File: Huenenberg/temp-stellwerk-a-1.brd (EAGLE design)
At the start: 99.1 x 61 mm, 117 parts, among them Q1 BSS123, Q10 BSS84, Q11 BSS123, Q12 BSS84, Q13 BSS123, Q14 BSS84, Q15 BSS123, Q16 BSS84, Q17 BSS123, Q18 BSS84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

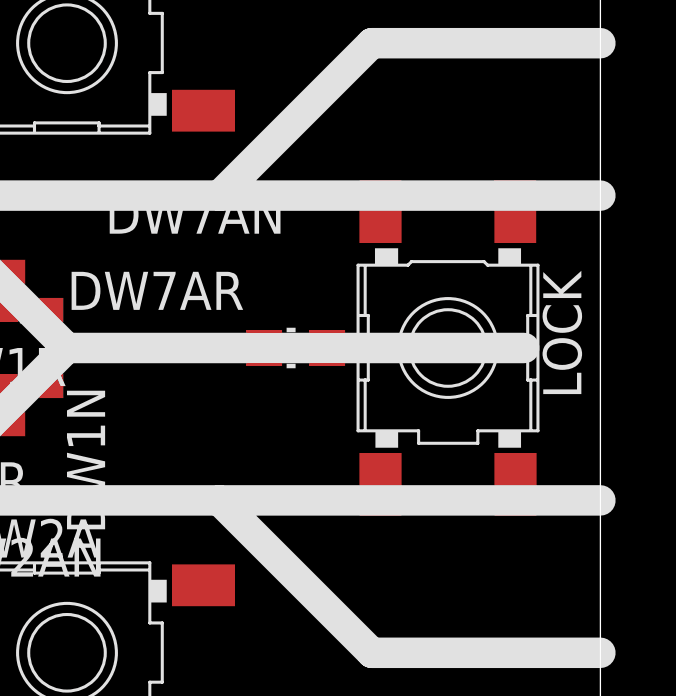
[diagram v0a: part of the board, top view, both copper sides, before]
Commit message: Updates names of all buttons.
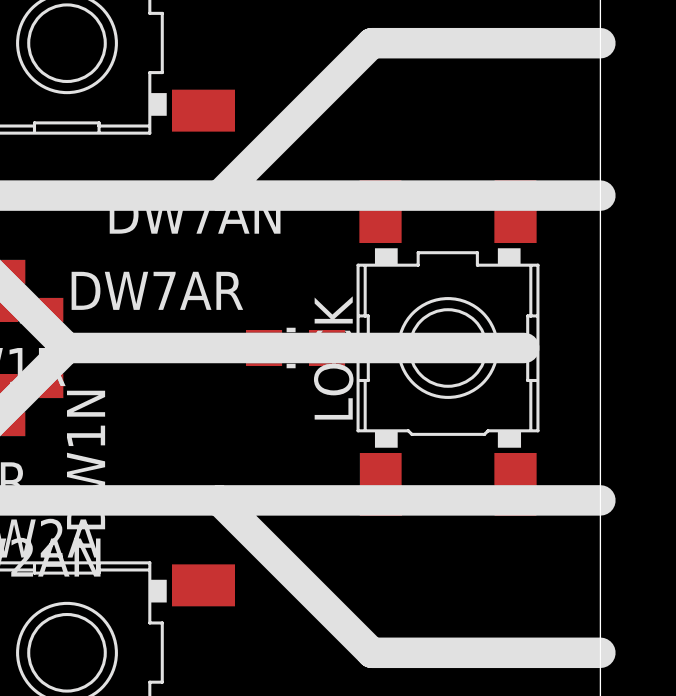
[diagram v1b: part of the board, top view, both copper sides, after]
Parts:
- LOCK: value W2 -> LOCK
- TRK1, TRK2, TRK3, TRK4, TRK5, TRK6, W2A, W7A: value W2 -> (none)
- W2B, W7B: value W1 -> (none)
- turned LOCK to 90 degrees
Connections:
- net CH10: now also Q11.1, Q12.1, R20.1; no longer Q25.1, R45.1
- net CH11: now also Q13.1, Q14.1, R23.1; no longer Q19.1, R34.1
- net CH12: now also Q15.1, Q16.1, R26.1; no longer Q20.1, R35.1
- net CH13: now also Q17.1, Q18.1, R30.1; no longer Q21.1, R37.1
- net CH14: now also Q24.1, R43.1; no longer Q22.1, R39.1
- net CH16: now also Q22.1, R39.1; no longer Q24.1, R43.1
- net CH6: now also Q19.1, R34.1; no longer Q11.1, Q12.1, R20.1
- net CH7: now also Q20.1, R35.1; no longer Q13.1, Q14.1, R23.1
- net CH8: now also Q21.1, R37.1; no longer Q15.1, Q16.1, R26.1
- net CH9: now also Q25.1, R45.1; no longer Q17.1, Q18.1, R30.1

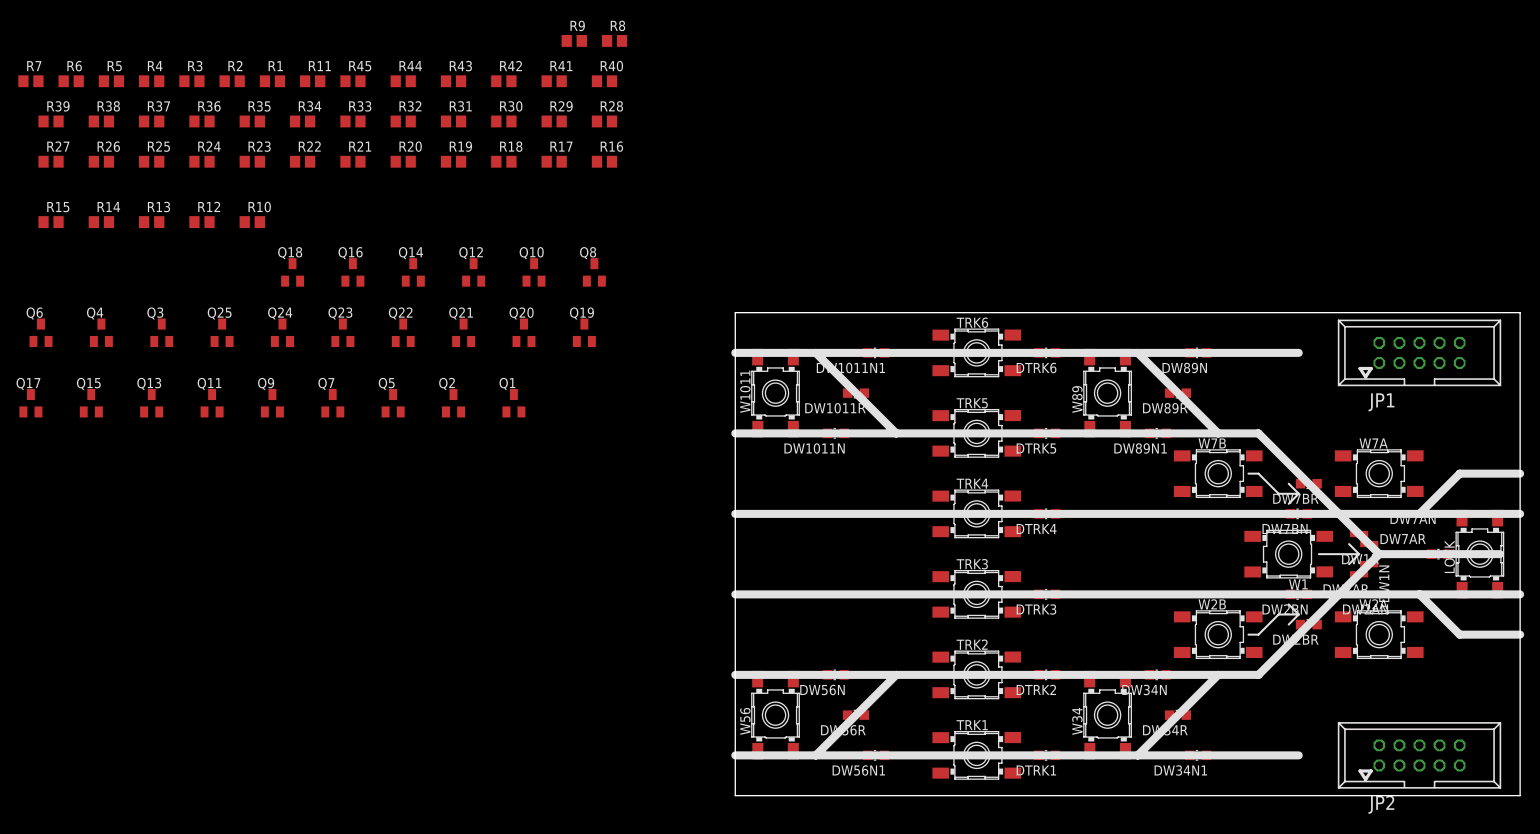
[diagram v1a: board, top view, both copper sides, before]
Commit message: Lays out all SMD parts on the bottom side.
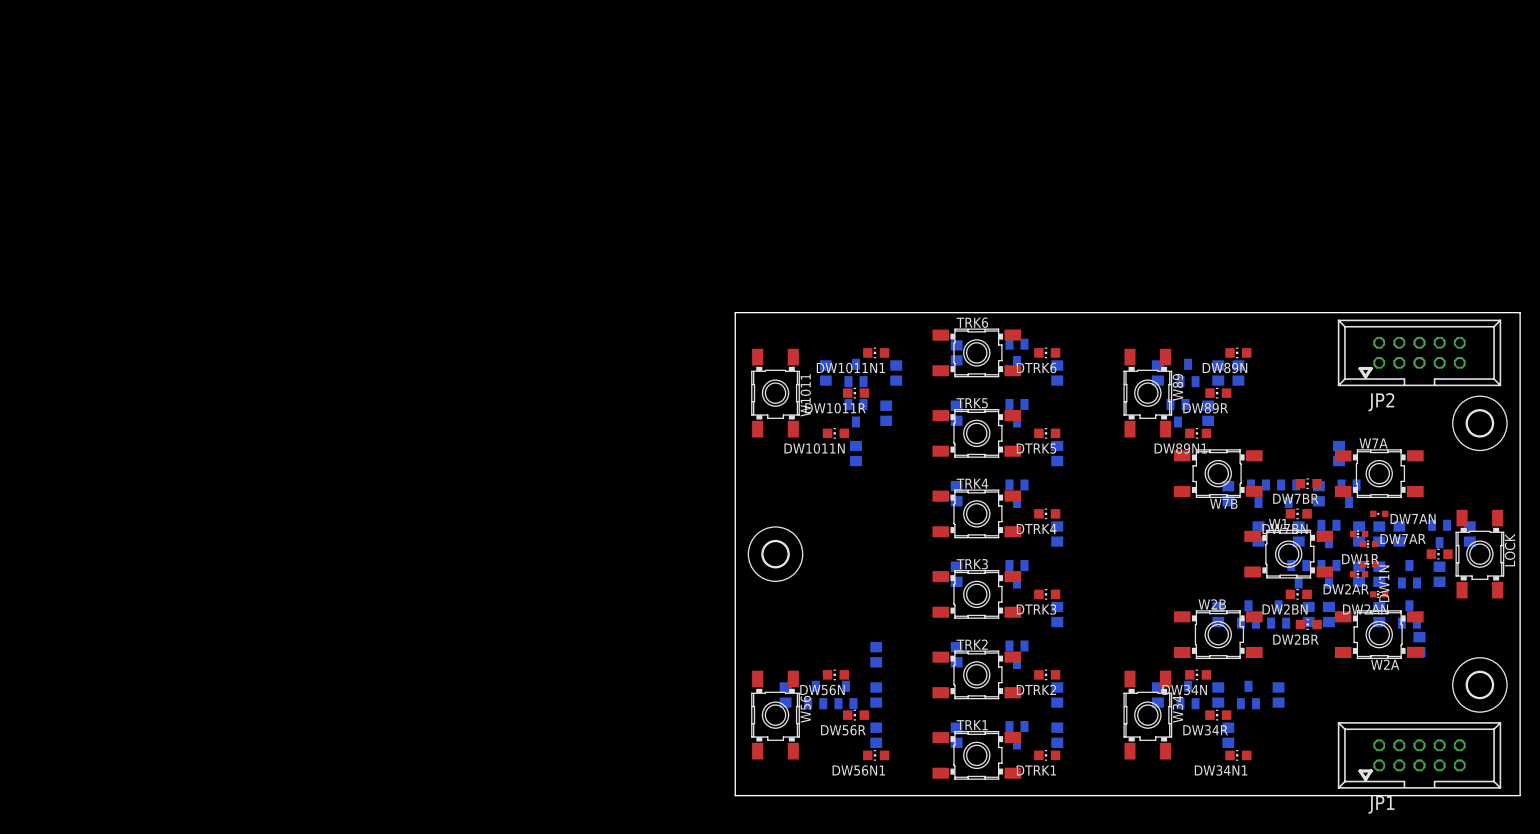
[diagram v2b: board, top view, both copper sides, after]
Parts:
- added H1, H2, H3: MOUNT-HOLE3.2, holes:3,2
- moved R6 184.4 mm to (86.4, 19.1), flipped to the bottom, turned to 270 degrees
- moved R7 177.1 mm to (74.9, 22.9), flipped to the bottom, turned to 270 degrees
- moved R5 171.7 mm to (81.3, 27.9), flipped to the bottom, turned to 270 degrees
- moved R4 168.9 mm to (81.3, 22.9), flipped to the bottom, turned to 270 degrees
- moved Q4 168.9 mm to (85.1, 22.9), flipped to the bottom
- moved Q6 160.2 mm to (68.6, 22.9), flipped to the bottom
- moved Q25 155.8 mm to (88.9, 33.0), flipped to the bottom, turned to 180 degrees
- moved R2 155.3 mm to (78.7, 27.9), flipped to the bottom, turned to 270 degrees
- moved R45 152.1 mm to (92.7, 33.0), flipped to the bottom, turned to 270 degrees
- moved R1 150.9 mm to (81.3, 33.0), flipped to the bottom, turned to 90 degrees
- moved R13 150.5 mm to (62.2, 7.62), flipped to the bottom, turned to 90 degrees
- moved Q3 150.4 mm to (74.9, 27.9), flipped to the bottom, turned to 180 degrees
- moved R27 149.5 mm to (59.7, 48.3), flipped to the bottom, turned to 90 degrees
- moved R3 146.2 mm to (66.0, 33.0), flipped to the bottom, turned to 90 degrees
- moved R44 144.9 mm to (88.9, 27.9), flipped to the bottom, turned to 270 degrees
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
